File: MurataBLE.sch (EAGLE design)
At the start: 48 parts, among them CON1 C-2235, IC1 I-5448, IC3 74LVC1G00DBV, IC4 IC_MEMORY_8P_AT25XE011_SOP, IC5 IC_MEMORY_8P_AT25XE011_TSSOP, Q1 FC-135 32.7680KA-AG3, U1 LBCA2HNZYZ-711, X1 C-04397

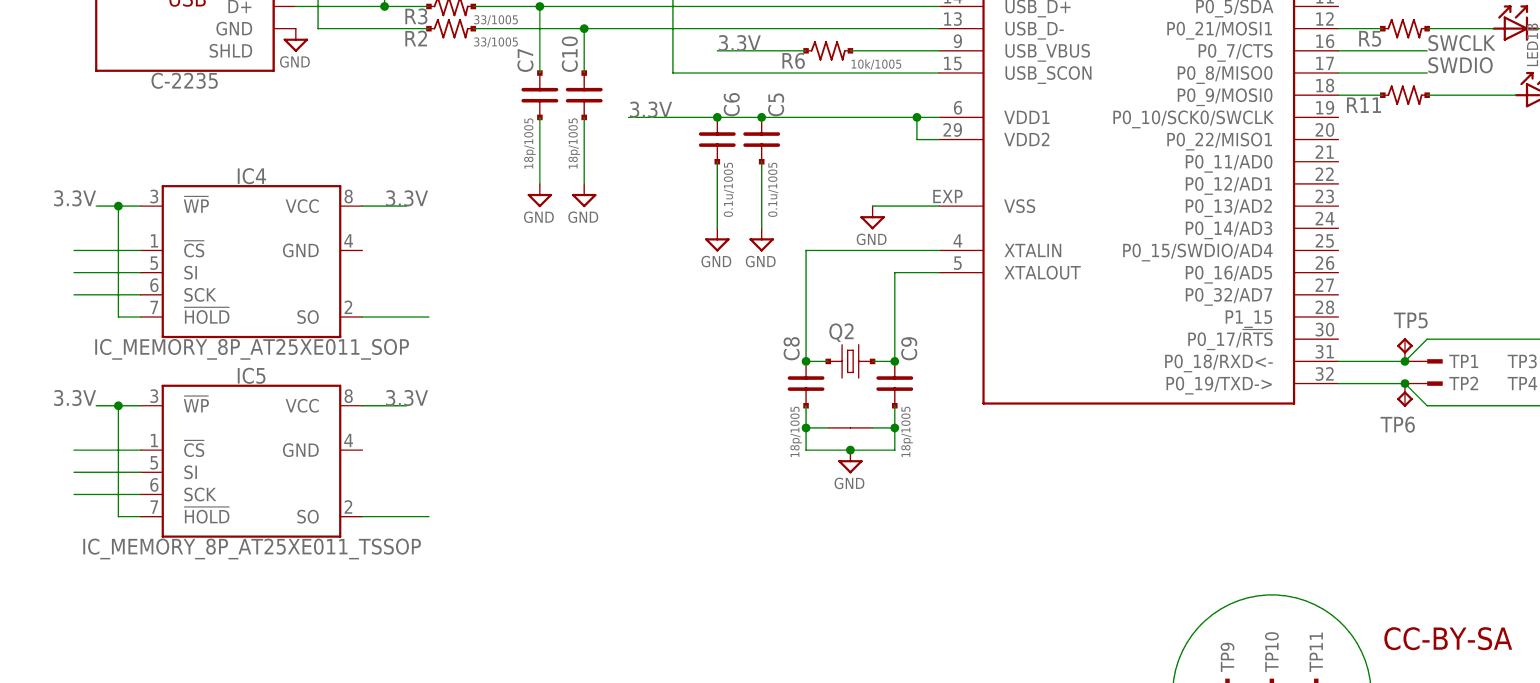
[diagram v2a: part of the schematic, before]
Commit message: [ USB ] SWSPI connections
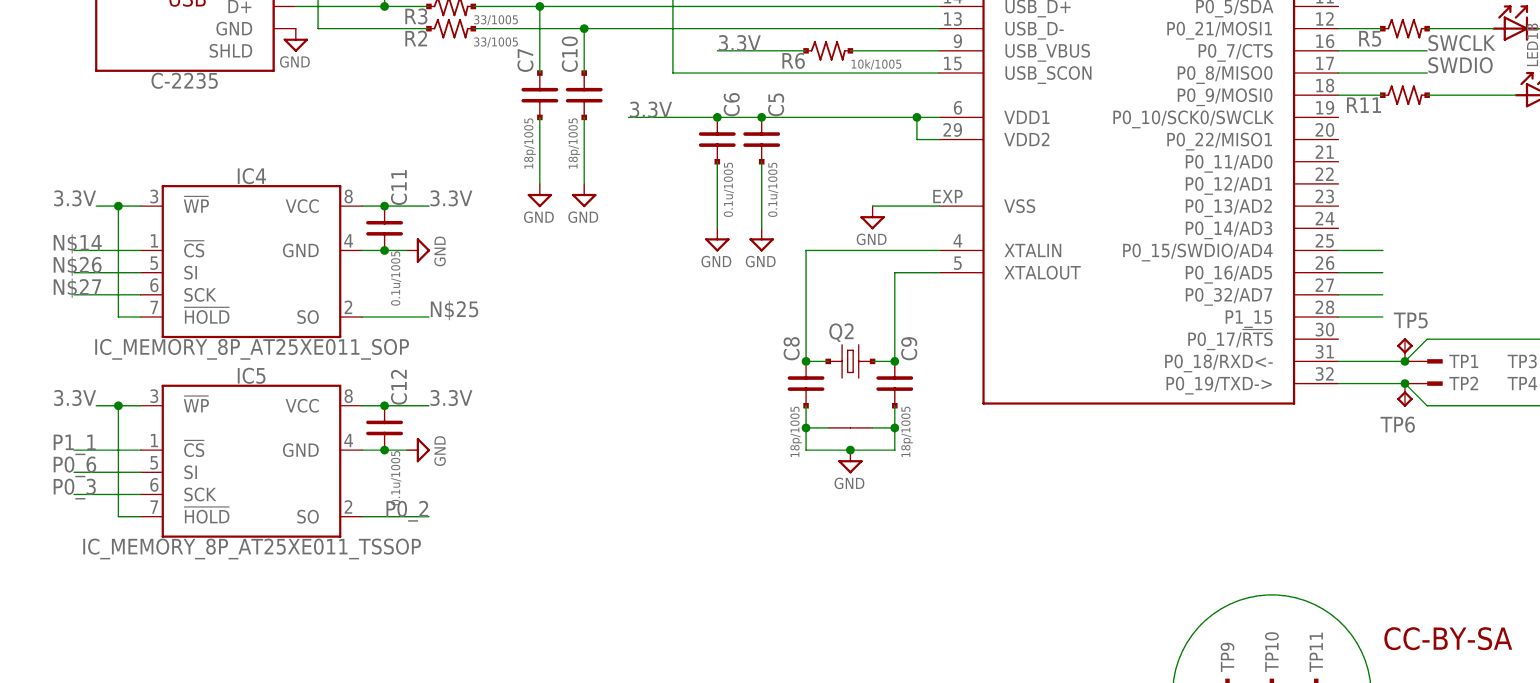
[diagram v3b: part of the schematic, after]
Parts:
- added C11, C12: 0.1u/1005, mylib:C_SMD_0.1U_1005
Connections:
- removed net N$15: IC4.!CS
- removed net N$16: IC4.SI
- removed net N$17: IC4.SCK
- removed net N$23: IC4.SO
- removed net N$28: IC5.SO
- new net N$14: IC2.P1_15, IC4.!CS
- net 3.3V: now also C11.1, C12.1, IC4.!HOLD, IC4.!WP
- net GND: now also C11.2, C12.2, IC4.GND, IC5.GND
- net N$25: now also IC2.P0_32/AD7, IC4.SO; no longer IC5.!CS
- net N$26: now also IC2.P0_16/AD5, IC4.SI; no longer IC5.SI
- net N$27: now also IC2.P0_15/SWDIO/AD4, IC4.SCK; no longer IC5.SCK
- net P0_2: now also IC5.SO
- net P0_3: now also IC5.SCK
- net P0_6: now also IC5.SI
- net P1_1: now also IC5.!CS
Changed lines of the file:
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@@
 <part name="IC5" library="mylib" deviceset="IC_MEMORY_8P_*" device="_TSSOP" technology="AT25XE011"/>
 <part name="IC2" library="mylib" deviceset="IC_LPC11U*_QFN33" device="_5X5" technology="35"/>
+<part name="SUPPLY17" library="mylib" deviceset="GND" device=""/>
+<part name="SUPPLY18" library="mylib" deviceset="GND" device=""/>
+<part name="C11" library="mylib" deviceset="C_SMD_*" device="_1005" technology="0.1U" value="0.1u/1005"/>
+<part name="C12" library="mylib" deviceset="C_SMD_*" device="_1005" technology="0.1U" value="0.1u/1005"/>
 </parts>
 <sheets>
@@
 <instance part="IC5" gate="G$1" x="33.02" y="40.64"/>
 <instance part="IC2" gate="G$1" x="134.62" y="111.76"/>
+<instance part="SUPPLY17" gate="GND" x="53.34" y="66.04" rot="R90"/>
+<instance part="SUPPLY18" gate="GND" x="53.34" y="43.18" rot="R90"/>
+<instance part="C11" gate="G$1" x="48.26" y="68.58"/>
+<instance part="C12" gate="G$1" x="48.26" y="45.72"/>
 </instances>
 <busses>
@@
 <pinref part="LED1" gate="B" pin="K"/>
 </segment>
+<segment>
+<pinref part="IC4" gate="G$1" pin="GND"/>
+<pinref part="SUPPLY17" gate="GND" pin="GND"/>
+<wire x1="50.8" y1="66.04" x2="48.26" y2="66.04" width="0.1524" layer="91"/>
+<pinref part="C11" gate="G$1" pin="2"/>
+<wire x1="48.26" y1="66.04" x2="45.72" y2="66.04" width="0.1524" layer="91"/>
+<junction x="48.26" y="66.04"/>
+</segment>
+<segment>
+<pinref part="IC5" gate="G$1" pin="GND"/>
+<pinref part="SUPPLY18" gate="GND" pin="GND"/>
+<wire x1="50.8" y1="43.18" x2="48.26" y2="43.18" width="0.1524" layer="91"/>
+<pinref part="C12" gate="G$1" pin="2"/>
+<wire x1="48.26" y1="43.18" x2="45.72" y2="43.18" width="0.1524" layer="91"/>
+<junction x="48.26" y="43.18"/>
+</segment>
 </net>
 <net name="N$2" class="0">
@@
 </segment>
 <segment>
-<wire x1="50.8" y1="71.12" x2="45.72" y2="71.12" width="0.1524" layer="91"/>
-<label x="48.26" y="71.12" size="1.778" layer="95"/>
+<wire x1="53.34" y1="71.12" x2="48.26" y2="71.12" width="0.1524" layer="91"/>
+<label x="53.34" y="71.12" size="1.778" layer="95"/>
 <pinref part="IC4" gate="G$1" pin="VCC"/>
-</segment>
-<segment>
-<wire x1="50.8" y1="48.26" x2="45.72" y2="48.26" width="0.1524" layer="91"/>
+<pinref part="C11" gate="G$1" pin="1"/>
+<wire x1="48.26" y1="71.12" x2="45.72" y2="71.12" width="0.1524" layer="91"/>
+<junction x="48.26" y="71.12"/>
+</segment>
+<segment>
+<wire x1="53.34" y1="48.26" x2="48.26" y2="48.26" width="0.1524" layer="91"/>
 <pinref part="IC5" gate="G$1" pin="VCC"/>
-<label x="48.26" y="48.26" size="1.778" layer="95"/>
+<label x="53.34" y="48.26" size="1.778" layer="95"/>
+<pinref part="C12" gate="G$1" pin="1"/>
+<wire x1="48.26" y1="48.26" x2="45.72" y2="48.26" width="0.1524" layer="91"/>
+<junction x="48.26" y="48.26"/>
 </segment>
 <segment>
@@
 <junction x="17.78" y="71.12"/>
 <label x="15.24" y="71.12" size="1.778" layer="95" rot="MR0"/>
+<pinref part="IC4" gate="G$1" pin="!HOLD"/>
+<pinref part="IC4" gate="G$1" pin="!WP"/>
 </segment>
 <segment>
@@
 <pinref part="X1" gate="-9" pin="1"/>
 </segment>
+<segment>
+<wire x1="12.7" y1="40.64" x2="20.32" y2="40.64" width="0.1524" layer="91"/>
+<pinref part="IC5" gate="G$1" pin="SI"/>
+<label x="10.16" y="40.64" size="1.778" layer="95"/>
+</segment>
 </net>
 <net name="P0_7" class="0">
@@
 <pinref part="X1" gate="-11" pin="1"/>
 </segment>
+<segment>
+<wire x1="53.34" y1="35.56" x2="45.72" y2="35.56" width="0.1524" layer="91"/>
+<pinref part="IC5" gate="G$1" pin="SO"/>
+<label x="48.26" y="35.56" size="1.778" layer="95"/>
+</segment>
 </net>
 <net name="P0_3" class="0">
@@
 <pinref part="X1" gate="-10" pin="1"/>
 </segment>
+<segment>
+<wire x1="20.32" y1="38.1" x2="12.7" y2="38.1" width="0.1524" layer="91"/>
+<pinref part="IC5" gate="G$1" pin="SCK"/>
+<label x="10.16" y="38.1" size="1.778" layer="95"/>
+</segment>
 </net>
 <net name="P0_4" class="0">
@@
 <pinref part="X1" gate="-12" pin="1"/>
 <label x="241.3" y="66.04" size="1.778" layer="95"/>
+</segment>
+<segment>
+<wire x1="20.32" y1="43.18" x2="12.7" y2="43.18" width="0.1524" layer="91"/>
+<pinref part="IC5" gate="G$1" pin="!CS"/>
+<label x="10.16" y="43.18" size="1.778" layer="95"/>
 </segment>
 </net>
@@
 </segment>
 </net>
-<net name="N$15" class="0">
-<segment>
+<net name="N$14" class="0">
+<segment>
+<pinref part="IC2" gate="G$1" pin="P1_15"/>
+<wire x1="157.48" y1="58.42" x2="162.56" y2="58.42" width="0.1524" layer="91"/>
+</segment>
+<segment>
+<wire x1="12.7" y1="66.04" x2="20.32" y2="66.04" width="0.1524" layer="91"/>
 <pinref part="IC4" gate="G$1" pin="!CS"/>
-<wire x1="20.32" y1="66.04" x2="12.7" y2="66.04" width="0.1524" layer="91"/>
-</segment>
-</net>
-<net name="N$16" class="0">
-<segment>
+<label x="10.16" y="66.04" size="1.778" layer="95"/>
+</segment>
+</net>
+<net name="N$25" class="0">
+<segment>
+<pinref part="IC2" gate="G$1" pin="P0_32/AD7"/>
+<wire x1="157.48" y1="60.96" x2="162.56" y2="60.96" width="0.1524" layer="91"/>
+</segment>
+<segment>
+<wire x1="45.72" y1="58.42" x2="53.34" y2="58.42" width="0.1524" layer="91"/>
+<pinref part="IC4" gate="G$1" pin="SO"/>
+<label x="53.34" y="58.42" size="1.778" layer="95"/>
+</segment>
+</net>
+<net name="N$26" class="0">
+<segment>
+<pinref part="IC2" gate="G$1" pin="P0_16/AD5"/>
+<wire x1="157.48" y1="63.5" x2="162.56" y2="63.5" width="0.1524" layer="91"/>
+</segment>
+<segment>
+<wire x1="12.7" y1="63.5" x2="20.32" y2="63.5" width="0.1524" layer="91"/>
 <pinref part="IC4" gate="G$1" pin="SI"/>
-<wire x1="20.32" y1="63.5" x2="12.7" y2="63.5" width="0.1524" layer="91"/>
-</segment>
-</net>
-<net name="N$17" class="0">
-<segment>
+<label x="10.16" y="63.5" size="1.778" layer="95"/>
+</segment>
+</net>
+<net name="N$27" class="0">
+<segment>
+<pinref part="IC2" gate="G$1" pin="P0_15/SWDIO/AD4"/>
+<wire x1="157.48" y1="66.04" x2="162.56" y2="66.04" width="0.1524" layer="91"/>
+</segment>
+<segment>
+<wire x1="12.7" y1="60.96" x2="20.32" y2="60.96" width="0.1524" layer="91"/>
 <pinref part="IC4" gate="G$1" pin="SCK"/>
-<wire x1="20.32" y1="60.96" x2="12.7" y2="60.96" width="0.1524" layer="91"/>
-</segment>
-</net>
-<net name="N$23" class="0">
-<segment>
-<pinref part="IC4" gate="G$1" pin="SO"/>
-<wire x1="45.72" y1="58.42" x2="53.34" y2="58.42" width="0.1524" layer="91"/>
-</segment>
-</net>
-<net name="N$25" class="0">
-<segment>
-<pinref part="IC5" gate="G$1" pin="!CS"/>
-<wire x1="20.32" y1="43.18" x2="12.7" y2="43.18" width="0.1524" layer="91"/>
-</segment>
-</net>
-<net name="N$26" class="0">
-<segment>
-<pinref part="IC5" gate="G$1" pin="SI"/>
-<wire x1="20.32" y1="40.64" x2="12.7" y2="40.64" width="0.1524" layer="91"/>
-</segment>
-</net>
-<net name="N$27" class="0">
-<segment>
-<pinref part="IC5" gate="G$1" pin="SCK"/>
-<wire x1="20.32" y1="38.1" x2="12.7" y2="38.1" width="0.1524" layer="91"/>
-</segment>
-</net>
-<net name="N$28" class="0">
-<segment>
-<pinref part="IC5" gate="G$1" pin="SO"/>
-<wire x1="45.72" y1="35.56" x2="53.34" y2="35.56" width="0.1524" layer="91"/>
-</segment>
-</net>
+<label x="10.16" y="60.96" size="1.778" layer="95"/>
+</segment>
+</net>

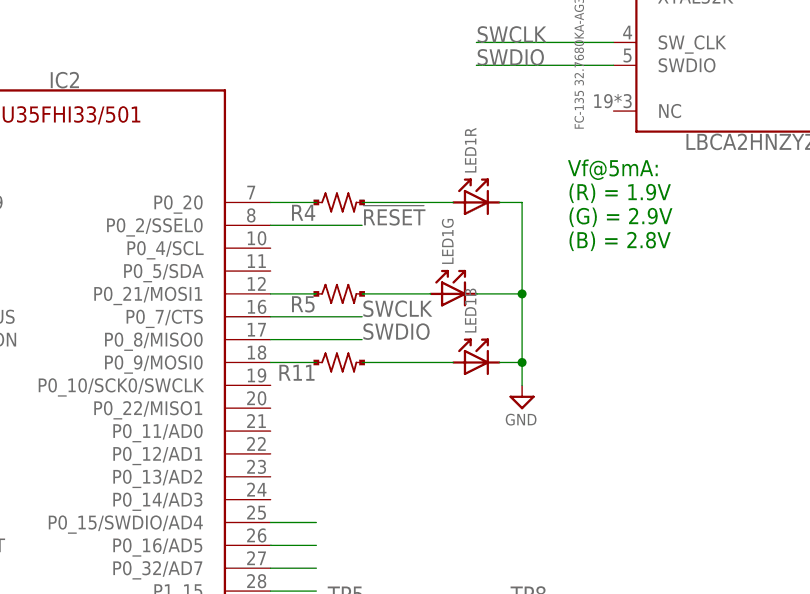
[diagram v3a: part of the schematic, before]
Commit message: [ USB ] LED connection; SWD connection removed from 11U35
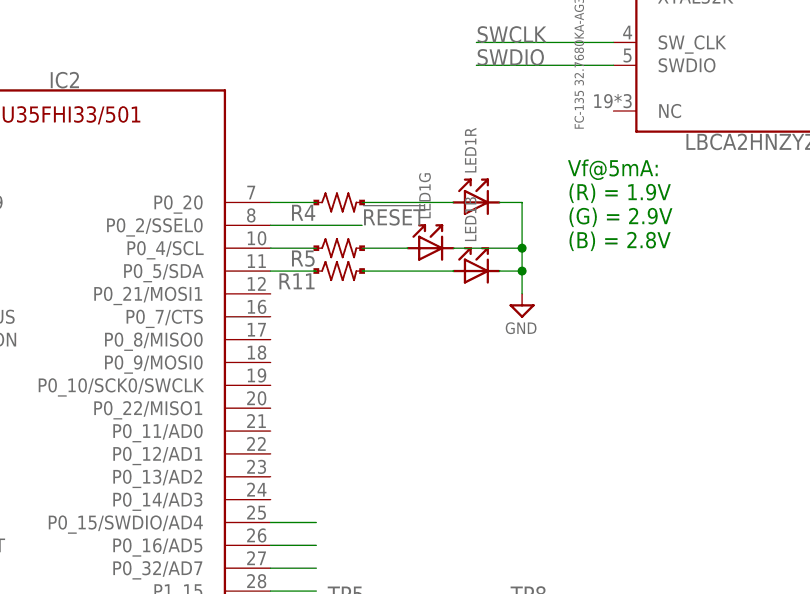
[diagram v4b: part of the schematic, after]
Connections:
- net N$10: now also IC2.P0_5/SDA; no longer IC2.P0_9/MOSI0
- net N$9: now also IC2.P0_4/SCL; no longer IC2.P0_21/MOSI1
- net SWCLK: no longer IC2.P0_7/CTS
- net SWDIO: no longer IC2.P0_8/MISO0
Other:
- moved on the sheet: LED1B, LED1G, R11, R5
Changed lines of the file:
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@@
 <instance part="IC3" gate="P" x="96.52" y="152.4"/>
 <instance part="R4" gate="G$1" x="165.1" y="101.6"/>
-<instance part="R5" gate="G$1" x="165.1" y="91.44"/>
-<instance part="R11" gate="G$1" x="165.1" y="83.82"/>
-<instance part="SUPPLY16" gate="GND" x="185.42" y="78.74"/>
+<instance part="R5" gate="G$1" x="165.1" y="96.52"/>
+<instance part="R11" gate="G$1" x="165.1" y="93.98"/>
+<instance part="SUPPLY16" gate="GND" x="185.42" y="88.9"/>
 <instance part="LED1" gate="R" x="180.34" y="101.6" rot="R90"/>
-<instance part="LED1" gate="G" x="177.8" y="91.44" rot="R90"/>
-<instance part="LED1" gate="B" x="180.34" y="83.82" rot="R90"/>
+<instance part="LED1" gate="G" x="175.26" y="96.52" rot="R90"/>
+<instance part="LED1" gate="B" x="180.34" y="93.98" rot="R90"/>
 <instance part="TP5" gate="G$1" x="165.1" y="55.88"/>
 <instance part="TP6" gate="G$1" x="165.1" y="48.26" rot="R180"/>
@@
 <segment>
 <wire x1="182.88" y1="101.6" x2="185.42" y2="101.6" width="0.1524" layer="91"/>
-<wire x1="185.42" y1="101.6" x2="185.42" y2="91.44" width="0.1524" layer="91"/>
-<wire x1="185.42" y1="91.44" x2="185.42" y2="83.82" width="0.1524" layer="91"/>
-<wire x1="185.42" y1="83.82" x2="185.42" y2="81.28" width="0.1524" layer="91"/>
-<wire x1="182.88" y1="83.82" x2="185.42" y2="83.82" width="0.1524" layer="91"/>
-<junction x="185.42" y="83.82"/>
-<wire x1="180.34" y1="91.44" x2="185.42" y2="91.44" width="0.1524" layer="91"/>
-<junction x="185.42" y="91.44"/>
+<wire x1="185.42" y1="101.6" x2="185.42" y2="96.52" width="0.1524" layer="91"/>
+<wire x1="185.42" y1="96.52" x2="185.42" y2="93.98" width="0.1524" layer="91"/>
+<wire x1="185.42" y1="93.98" x2="185.42" y2="91.44" width="0.1524" layer="91"/>
+<wire x1="182.88" y1="93.98" x2="185.42" y2="93.98" width="0.1524" layer="91"/>
+<junction x="185.42" y="93.98"/>
+<wire x1="177.8" y1="96.52" x2="185.42" y2="96.52" width="0.1524" layer="91"/>
+<junction x="185.42" y="96.52"/>
 <pinref part="SUPPLY16" gate="GND" pin="GND"/>
 <pinref part="LED1" gate="R" pin="K"/>
@@
 </segment>
 <segment>
-<label x="167.64" y="88.9" size="1.778" layer="95"/>
-<wire x1="157.48" y1="88.9" x2="167.64" y2="88.9" width="0.1524" layer="91"/>
-<pinref part="IC2" gate="G$1" pin="P0_7/CTS"/>
-</segment>
-<segment>
 <label x="241.3" y="93.98" size="1.778" layer="95"/>
 <wire x1="233.68" y1="93.98" x2="241.3" y2="93.98" width="0.1524" layer="91"/>
@@
 <net name="SWDIO" class="0">
 <segment>
-<label x="167.64" y="86.36" size="1.778" layer="95"/>
-<wire x1="157.48" y1="86.36" x2="167.64" y2="86.36" width="0.1524" layer="91"/>
-<pinref part="IC2" gate="G$1" pin="P0_8/MISO0"/>
-</segment>
-<segment>
 <pinref part="U1" gate="G$1" pin="SWDIO"/>
 <wire x1="195.58" y1="116.84" x2="180.34" y2="116.84" width="0.1524" layer="91"/>
@@
 <segment>
 <pinref part="R5" gate="G$1" pin="1"/>
-<wire x1="157.48" y1="91.44" x2="162.56" y2="91.44" width="0.1524" layer="91"/>
-<pinref part="IC2" gate="G$1" pin="P0_21/MOSI1"/>
+<pinref part="IC2" gate="G$1" pin="P0_4/SCL"/>
+<wire x1="157.48" y1="96.52" x2="162.56" y2="96.52" width="0.1524" layer="91"/>
 </segment>
 </net>
@@
 <segment>
 <pinref part="R11" gate="G$1" pin="1"/>
-<wire x1="157.48" y1="83.82" x2="162.56" y2="83.82" width="0.1524" layer="91"/>
-<pinref part="IC2" gate="G$1" pin="P0_9/MOSI0"/>
+<pinref part="IC2" gate="G$1" pin="P0_5/SDA"/>
+<wire x1="157.48" y1="93.98" x2="162.56" y2="93.98" width="0.1524" layer="91"/>
 </segment>
 </net>
@@
 <segment>
 <pinref part="R5" gate="G$1" pin="2"/>
-<wire x1="175.26" y1="91.44" x2="167.64" y2="91.44" width="0.1524" layer="91"/>
+<wire x1="172.72" y1="96.52" x2="167.64" y2="96.52" width="0.1524" layer="91"/>
 <pinref part="LED1" gate="G" pin="A"/>
 </segment>
@@
 <segment>
 <pinref part="R11" gate="G$1" pin="2"/>
-<wire x1="167.64" y1="83.82" x2="177.8" y2="83.82" width="0.1524" layer="91"/>
+<wire x1="167.64" y1="93.98" x2="177.8" y2="93.98" width="0.1524" layer="91"/>
 <pinref part="LED1" gate="B" pin="A"/>
 </segment>
